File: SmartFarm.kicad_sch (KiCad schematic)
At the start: 39 parts, among them J1 Conn_01x20_Pin, J10 Conn_01x06_Socket, J11 Conn_01x06_Socket, J12 Conn_01x01_Pin, J13 Conn_01x01_Pin, J14 Conn_01x01_Pin, J15 Conn_01x01_Pin, J16 Screw_Terminal_01x02, J2 Conn_01x20_Pin, J4 Conn_01x04, J5 Screw_Terminal_01x03, J6 Conn_01x01_Pin, J7 Screw_Terminal_01x03, J8 Barrel_Jack, J9 Screw_Terminal_01x03, M1 Fan, Q1 2N3904, SW1 SW_DIP_x01, SW2 SW_MEC_5E, SW3 SW_MEC_5E

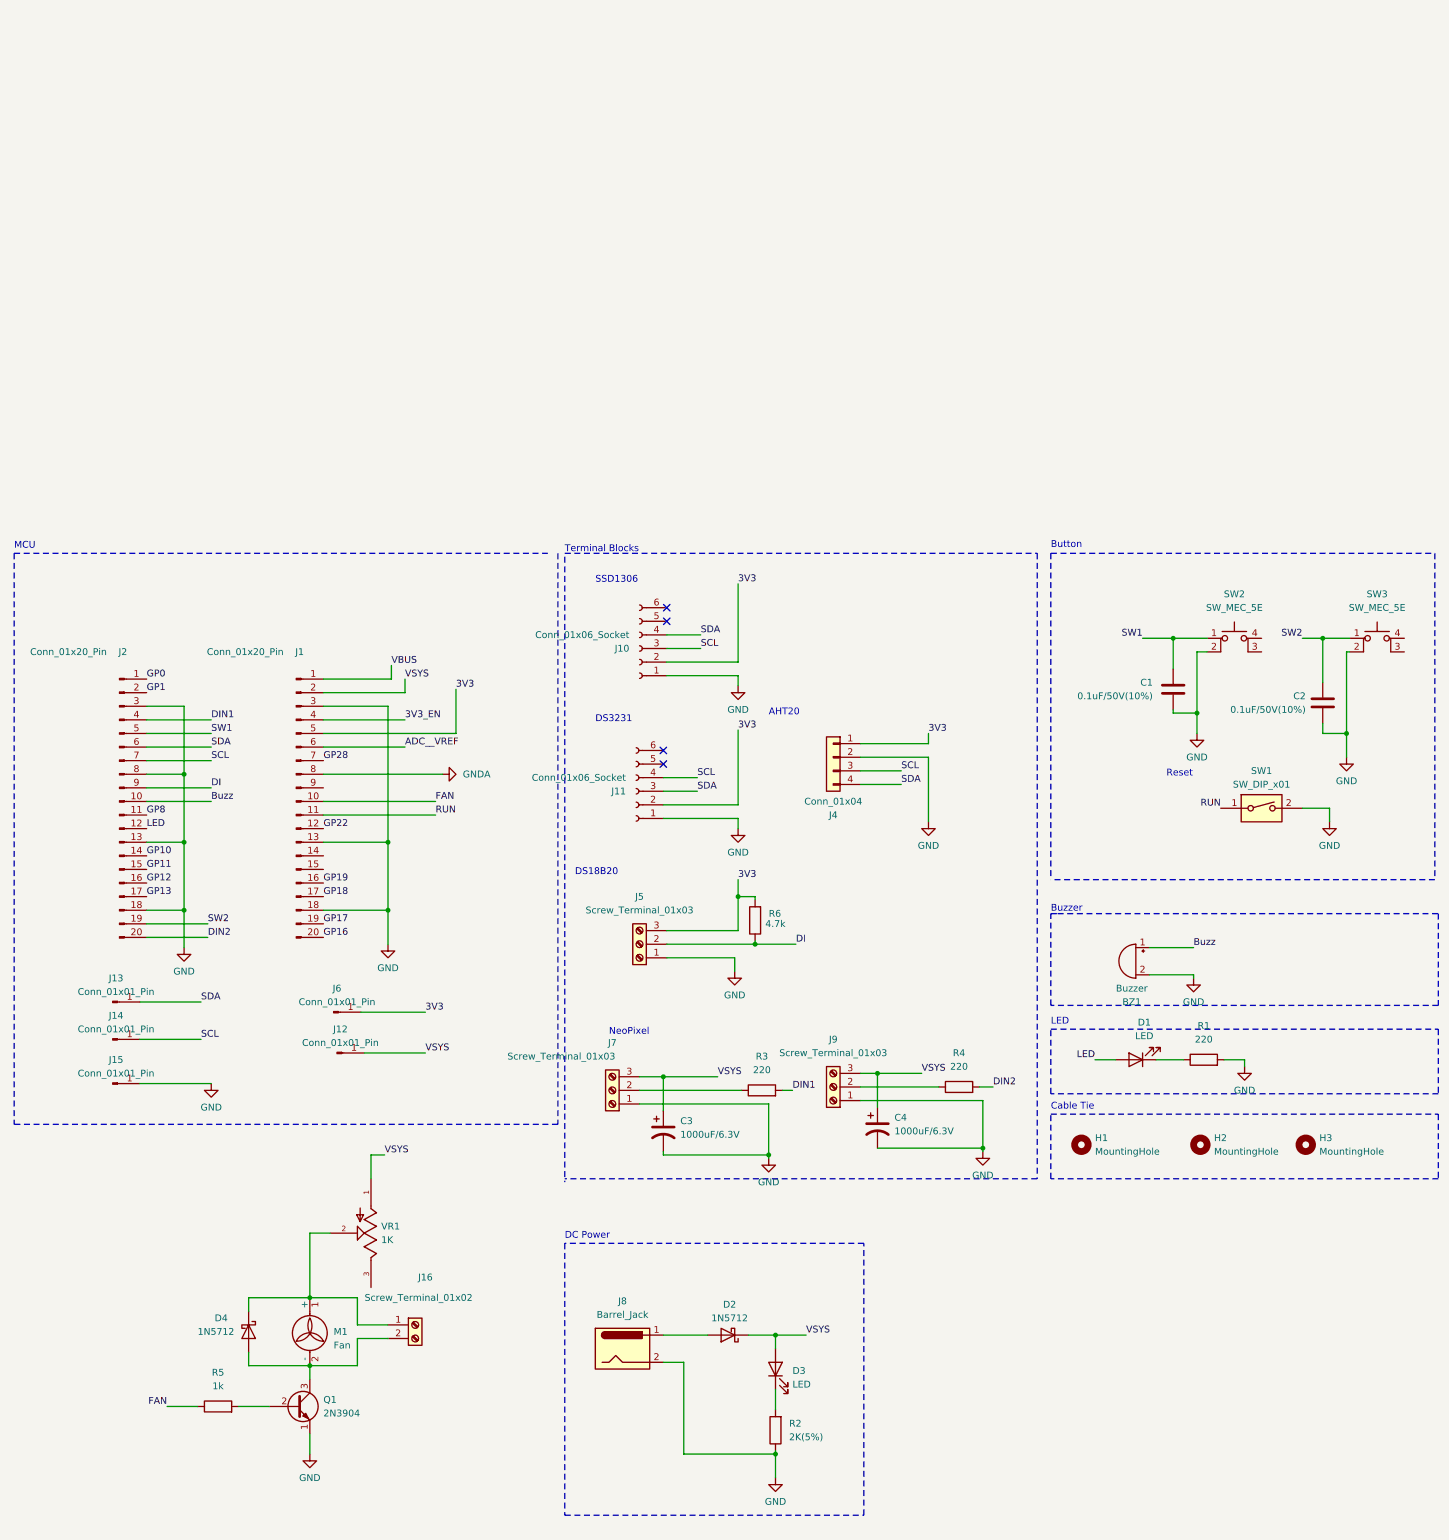
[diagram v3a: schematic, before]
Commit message: add pico w board
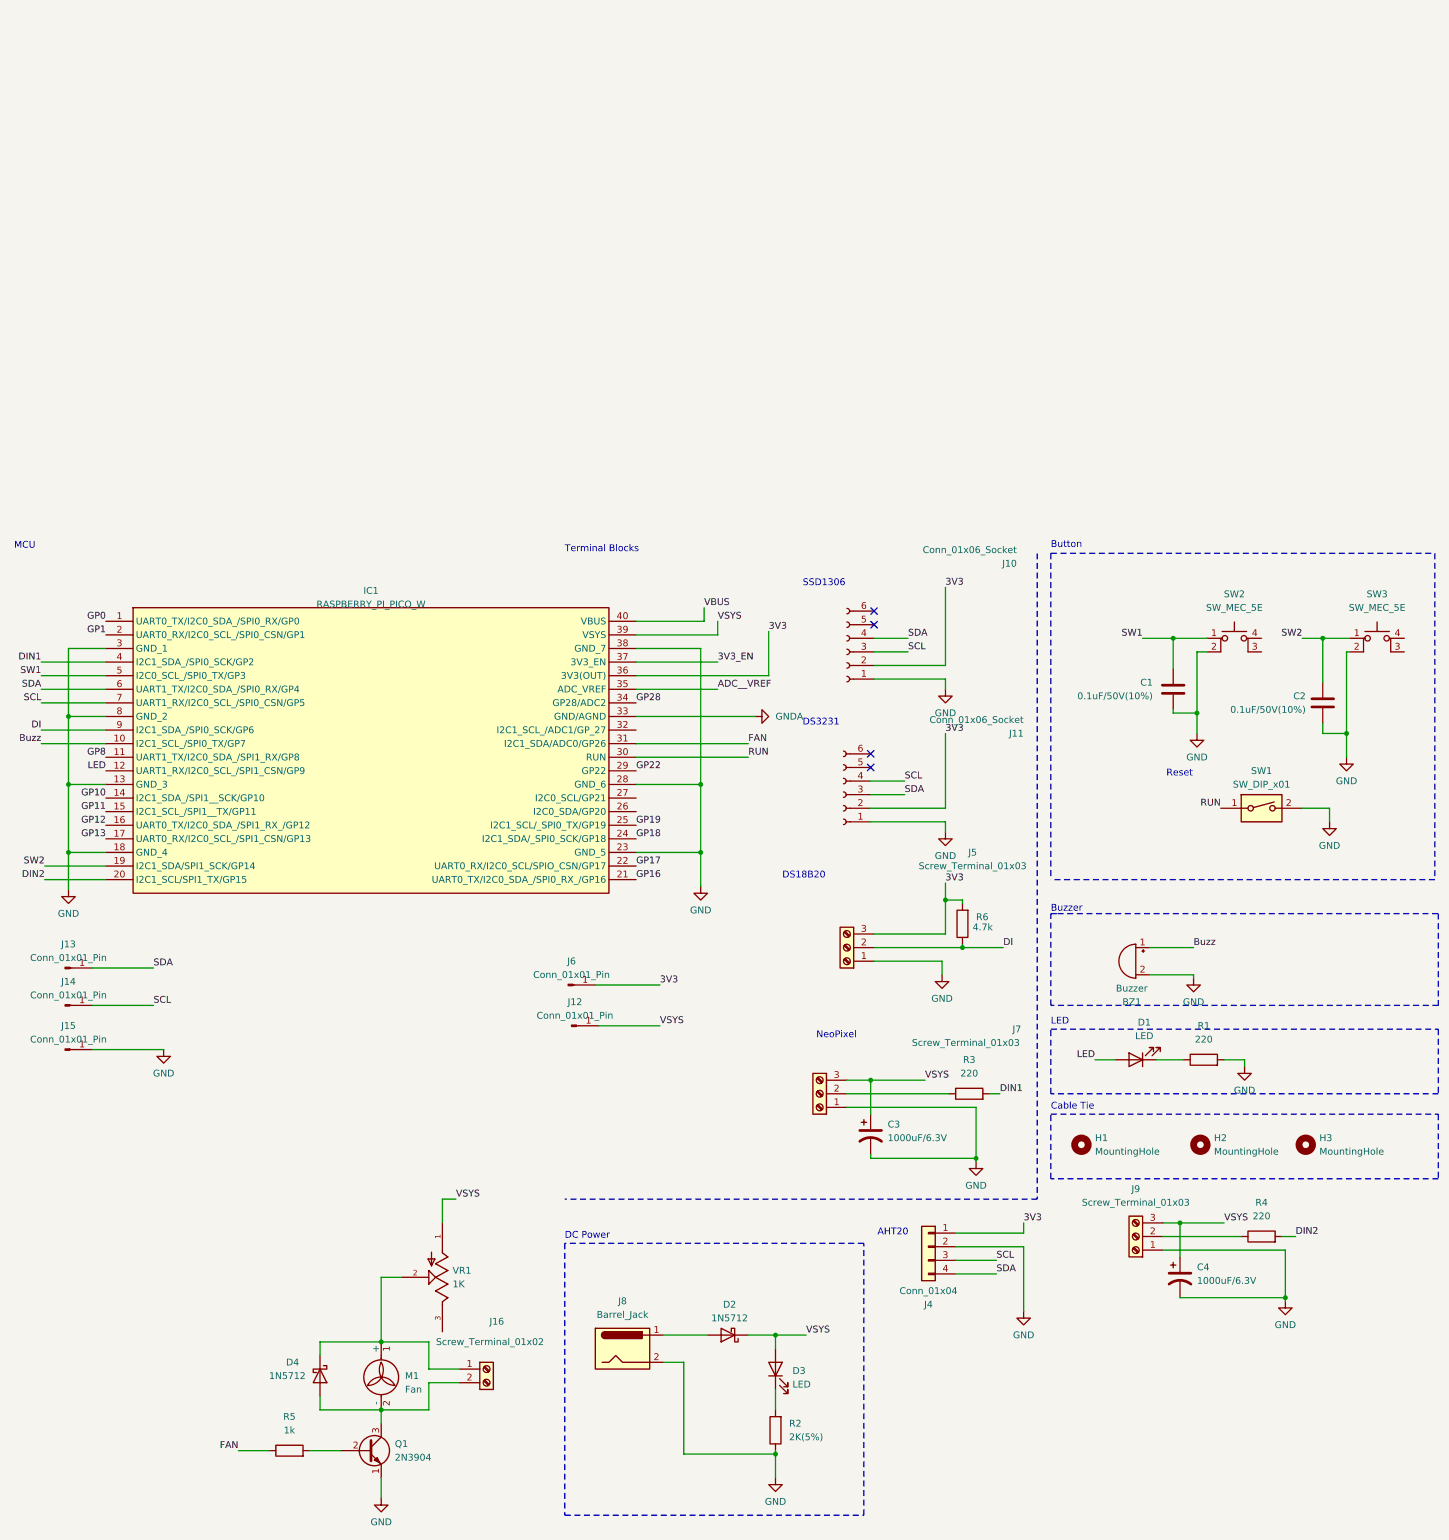
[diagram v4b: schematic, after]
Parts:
- removed J1, J2: Conn_01x20_Pin, Connector_PinSocket_2.54mm:PinSocket_1x20_P2.54mm_Vertical, symbol Connector:Conn_01x20_Pin
- added IC1: RASPBERRY_PI_PICO_W, RASPBERRYPIPICOW, symbol RASPBERRY_PI_PICO_W:RASPBERRY_PI_PICO_W
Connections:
- net 3V3: now also IC1.36 (3V3(OUT))
- net 3V3_EN: now also IC1.37 (3V3_EN)
- net ADC__VREF: now also IC1.35 (ADC_VREF)
- net Buzz: now also IC1.10 (I2C1_SCL_/SPI0_TX/GP7)
- net DI: now also IC1.9 (I2C1_SDA_/SPI0_SCK/GP6)
- net DIN1: now also IC1.4 (I2C1_SDA_/SPI0_SCK/GP2)
- net DIN2: now also IC1.20 (I2C1_SCL/SPI1_TX/GP15)
- net FAN: now also IC1.31 (I2C1_SDA/ADC0/GP26)
- net GND: now also IC1.13 (GND_3), IC1.18 (GND_4), IC1.23 (GND_5), IC1.28 (GND_6), IC1.3 (GND_1), IC1.38 (GND_7), IC1.8 (GND_2)
- net GNDA: now also IC1.33 (GND/AGND)
- net GP0: now also IC1.1 (UART0_TX/I2C0_SDA_/SPI0_RX/GP0)
- net GP1: now also IC1.2 (UART0_RX/I2C0_SCL_/SPI0_CSN/GP1)
- net GP10: now also IC1.14 (I2C1_SDA_/SPI1__SCK/GP10)
- net GP11: now also IC1.15 (I2C1_SCL_/SPI1__TX/GP11)
- net GP12: now also IC1.16 (UART0_TX/I2C0_SDA_/SPI1_RX_/GP12)
- net GP13: now also IC1.17 (UART0_RX/I2C0_SCL_/SPI1_CSN/GP13)
- net GP16: now also IC1.21 (UART0_TX/I2C0_SDA_/SPI0_RX_/GP16)
- net GP17: now also IC1.22 (UART0_RX/I2C0_SCL/SPIO_CSN/GP17)
- net GP18: now also IC1.24 (I2C1_SDA/_SPI0_SCK/GP18)
- net GP19: now also IC1.25 (I2C1_SCL/_SPI0_TX/GP19)
- net GP22: now also IC1.29 (GP22)
- net GP28: now also IC1.34 (GP28/ADC2)
- net GP8: now also IC1.11 (UART1_TX/I2C0_SDA_/SPI1_RX/GP8)
- net LED: now also IC1.12 (UART1_RX/I2C0_SCL_/SPI1_CSN/GP9)
- net RUN: now also IC1.30 (RUN)
- net SCL: now also IC1.7 (UART1_RX/I2C0_SCL_/SPI0_CSN/GP5)
- net SDA: now also IC1.6 (UART1_TX/I2C0_SDA_/SPI0_RX/GP4)
- net SW1: now also IC1.5 (I2C0_SCL_/SPI0_TX/GP3)
- net SW2: now also IC1.19 (I2C1_SDA/SPI1_SCK/GP14)
- net VBUS: now also IC1.40 (VBUS)
- net VSYS: now also IC1.39 (VSYS)
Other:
- moved on the sheet: C3, C4, D4, J10, J11, J12, J13, J14, J15, J16, J4, J5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

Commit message: add smd library parts
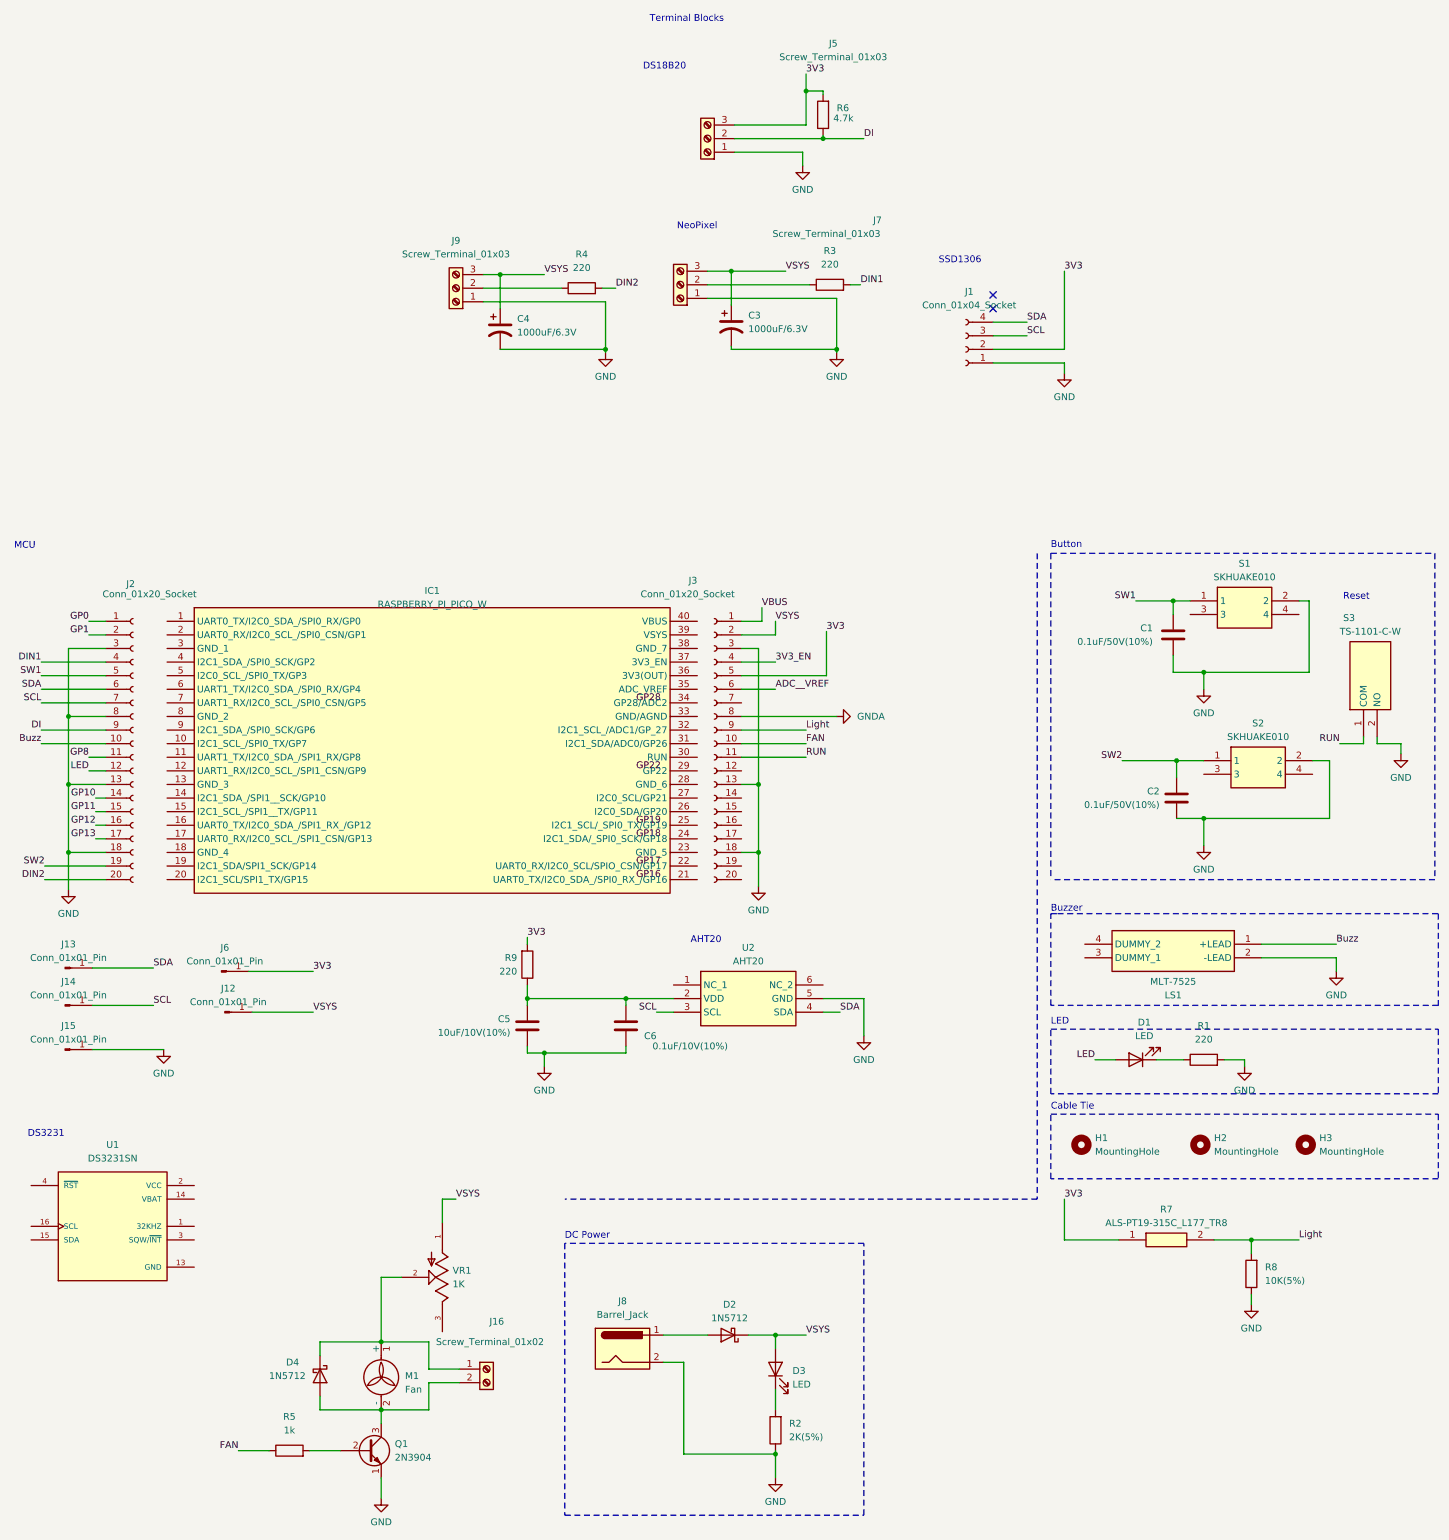
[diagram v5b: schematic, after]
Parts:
- removed BZ1: Buzzer, Buzzer_Beeper:Buzzer_12x9.5RM7.6, symbol Device:Buzzer
- removed J10, J11: Conn_01x06_Socket, Connector_PinSocket_2.54mm:PinSocket_1x06_P2.54mm_Vertical, symbol Connector:Conn_01x06_Socket
- removed J4: Conn_01x04, Connector_PinSocket_2.54mm:PinSocket_1x04_P2.54mm_Vertical, symbol Connector_Generic:Conn_01x04
- removed SW1: SW_DIP_x01, Button_Switch_THT:SW_PUSH_1P1T_6x3.5mm_H4.3_APEM_MJTP1243, symbol Switch:SW_DIP_x01
- removed SW2, SW3: SW_MEC_5E, Button_Switch_THT:SW_TH_Tactile_Omron_B3F-10xx, symbol Switch:SW_MEC_5E
- added C5: 10uF/10V(10%), Capacitor_Tantalum_SMD:CP_EIA-1608-10_AVX-L_Pad1.25x1.05mm_HandSolder, symbol Device:C
- added C6: 0.1uF/10V(10%), Capacitor_Tantalum_SMD:CP_EIA-1608-10_AVX-L_Pad1.25x1.05mm_HandSolder, symbol Device:C
- added J1: Conn_01x04_Socket, Connector_PinHeader_2.54mm:PinHeader_1x04_P2.54mm_Vertical_SMD_Pin1Left, symbol Connector:Conn_01x04_Socket
- added J2: Conn_01x20_Socket, Connector_PinSocket_2.54mm:PinSocket_1x20_P2.54mm_Vertical_SMD_Pin1Left, symbol Connector:Conn_01x20_Socket
- added J3: Conn_01x20_Socket, Connector_PinSocket_2.54mm:PinSocket_1x20_P2.54mm_Vertical_SMD_Pin1Right, symbol Connector:Conn_01x20_Socket
- added LS1: MLT-7525, MLT7525, symbol MLT-7525:MLT-7525
- added R7: ALS-PT19-315C_L177_TR8, ALSPT19315CL177TR8, symbol ALS-PT19-315C_L177_TR8:ALS-PT19-315C_L177_TR8
- added R8: 10K(5%), Resistor_SMD:R_0603_1608Metric_Pad0.98x0.95mm_HandSolder, symbol Device:R
- added R9: 220, Resistor_SMD:R_0603_1608Metric_Pad0.98x0.95mm_HandSolder, symbol Device:R
- added S1, S2: SKHUAKE010, SKHUAKE010, symbol SKHUAKE010:SKHUAKE010
- added S3: TS-1101-C-W, TS1101CW, symbol TS-1101-C-W:TS-1101-C-W
- added U1: DS3231SN, DS3231SN:SOIC127P1032X265-16N, symbol DS3231SN:DS3231SN
- added U2: AHT20, AHT20, symbol AHT20:AHT20
- C1, C2: footprint Capacitor_THT:C_Disc_D3.0mm_W1.6mm_P2.50mm -> Capacitor_Tantalum_SMD:CP_EIA-1608-08_AVX-J_Pad1.25x1.05mm_HandSolder
- C3, C4: footprint Capacitor_THT:CP_Radial_D8.0mm_P5.00mm -> EEEHAA102UAP:EEE0JA152UAP
- D1, D3: footprint LED_THT:LED_D3.0mm -> LED_SMD:LED_0603_1608Metric_Pad1.05x0.95mm_HandSolder
- D2, D4: footprint Diode_THT:D_DO-35_SOD27_P10.16mm_Horizontal -> 1N5711W-7-F:SOD3716X115N
- IC1: now left out of the parts list
- Q1: footprint Package_TO_SOT_THT:TO-92_Inline -> 2N3904S-RTK:2N3904SRTKPS
- R1, R2, R5: footprint Resistor_THT:R_Axial_DIN0204_L3.6mm_D1.6mm_P5.08mm_Horizontal -> Resistor_SMD:R_0603_1608Metric_Pad0.98x0.95mm_HandSolder
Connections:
- net 3V3: now also J1.2 (Pin_2), J3.5 (Pin_5), R7.1 (COLLECTOR), R9.2; no longer IC1.36 (3V3(OUT))
- net 3V3_EN: now also J3.4 (Pin_4); no longer IC1.37 (3V3_EN)
- net ADC__VREF: now also J3.6 (Pin_6); no longer IC1.35 (ADC_VREF)
- net Buzz: now also J2.10 (Pin_10), LS1.1 (+LEAD); no longer IC1.10 (I2C1_SCL_/SPI0_TX/GP7)
- net DI: now also J2.9 (Pin_9); no longer IC1.9 (I2C1_SDA_/SPI0_SCK/GP6)
- net DIN1: now also J2.4 (Pin_4); no longer IC1.4 (I2C1_SDA_/SPI0_SCK/GP2)
- net DIN2: now also J2.20 (Pin_20); no longer IC1.20 (I2C1_SCL/SPI1_TX/GP15)
- net FAN: now also J3.10 (Pin_10); no longer IC1.31 (I2C1_SDA/ADC0/GP26)
- net GND: now also C5.1, C6.1, J1.1 (Pin_1), J2.13 (Pin_13), J2.18 (Pin_18), J2.3 (Pin_3), J2.8 (Pin_8), J3.13 (Pin_13), J3.18 (Pin_18), J3.3 (Pin_3), LS1.2 (-LEAD), R8.1, S1.2, S2.2, S3.2 (NO), U2.5 (GND); no longer IC1.13 (GND_3), IC1.18 (GND_4), IC1.23 (GND_5), IC1.28 (GND_6), IC1.3 (GND_1), IC1.38 (GND_7), IC1.8 (GND_2)
- net GNDA: now also J3.8 (Pin_8); no longer IC1.33 (GND/AGND)
- net GP0: now also J2.1 (Pin_1); no longer IC1.1 (UART0_TX/I2C0_SDA_/SPI0_RX/GP0)
- net GP1: now also J2.2 (Pin_2); no longer IC1.2 (UART0_RX/I2C0_SCL_/SPI0_CSN/GP1)
- net GP10: now also J2.14 (Pin_14); no longer IC1.14 (I2C1_SDA_/SPI1__SCK/GP10)
- net GP11: now also J2.15 (Pin_15); no longer IC1.15 (I2C1_SCL_/SPI1__TX/GP11)
- net GP12: now also J2.16 (Pin_16); no longer IC1.16 (UART0_TX/I2C0_SDA_/SPI1_RX_/GP12)
- net GP13: now also J2.17 (Pin_17); no longer IC1.17 (UART0_RX/I2C0_SCL_/SPI1_CSN/GP13)
- net GP16: no longer IC1.21 (UART0_TX/I2C0_SDA_/SPI0_RX_/GP16)
- net GP17: no longer IC1.22 (UART0_RX/I2C0_SCL/SPIO_CSN/GP17)
- net GP18: no longer IC1.24 (I2C1_SDA/_SPI0_SCK/GP18)
- net GP19: no longer IC1.25 (I2C1_SCL/_SPI0_TX/GP19)
- net GP22: no longer IC1.29 (GP22)
- net GP28: no longer IC1.34 (GP28/ADC2)
- net GP8: now also J2.11 (Pin_11); no longer IC1.11 (UART1_TX/I2C0_SDA_/SPI1_RX/GP8)
- net LED: now also J2.12 (Pin_12); no longer IC1.12 (UART1_RX/I2C0_SCL_/SPI1_CSN/GP9)
- net RUN: now also J3.11 (Pin_11), S3.1 (COM); no longer IC1.30 (RUN)
- net SCL: now also J1.3 (Pin_3), J2.7 (Pin_7), U2.3 (SCL); no longer IC1.7 (UART1_RX/I2C0_SCL_/SPI0_CSN/GP5)
- net SDA: now also J1.4 (Pin_4), J2.6 (Pin_6), U2.4 (SDA); no longer IC1.6 (UART1_TX/I2C0_SDA_/SPI0_RX/GP4)
- net SW1: now also J2.5 (Pin_5), S1.1; no longer IC1.5 (I2C0_SCL_/SPI0_TX/GP3)
- net SW2: now also J2.19 (Pin_19), S2.1; no longer IC1.19 (I2C1_SDA/SPI1_SCK/GP14)
- net VBUS: now also J3.1 (Pin_1); no longer IC1.40 (VBUS)
- net VSYS: now also J3.2 (Pin_2); no longer IC1.39 (VSYS)
- new net: C5.2, C6.2, R9.1, U2.2 (VDD)
- new net Light: J3.9 (Pin_9), R7.2 (EMITTER), R8.2
- no-connect marks 4 -> 2
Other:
- moved on the sheet: C1, C2, C3, C4, IC1, J12, J5, J6, J7, J9, R3, R4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
